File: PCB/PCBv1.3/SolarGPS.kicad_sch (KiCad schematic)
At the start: 65 parts, among them J1 Conn_01x24_Female, J2 GND, J3 GND, J4 Conn_02x03_Odd_Even, J5 Solar2+, J6 Solar1+, J7 Screw_Terminal_01x01, J8 Conn_01x04_Male, Q1 Q_NMOS_GSD, U1 STM32L011G4Ux, U2 MAX-M10Q, U3 BQ25570, U6 LIS3DH, Y1 32.768

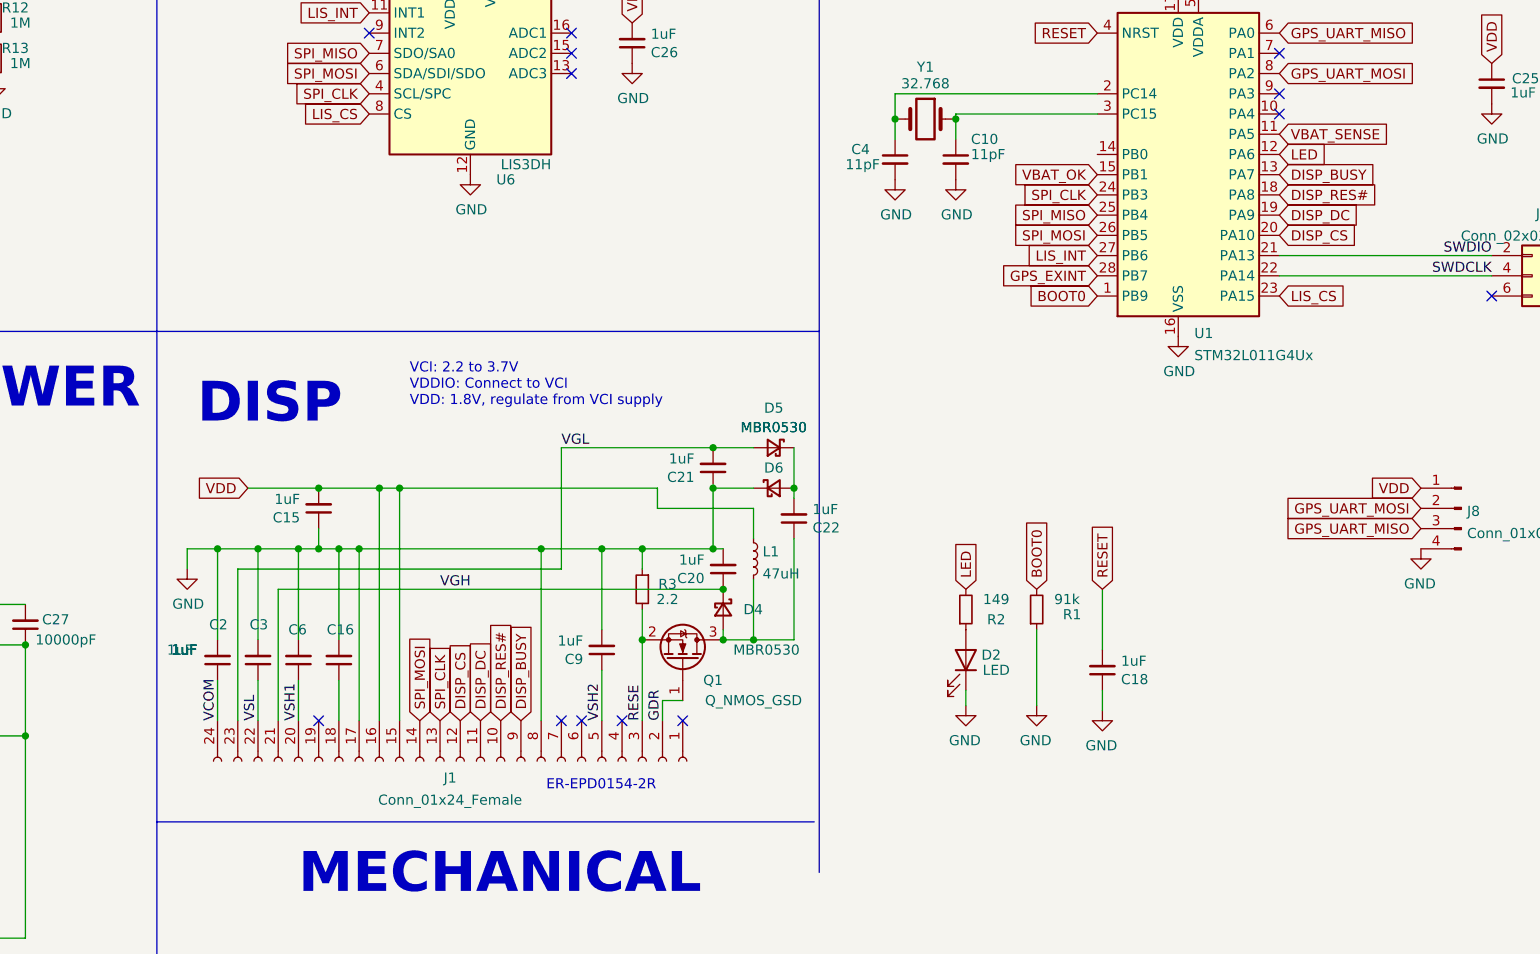
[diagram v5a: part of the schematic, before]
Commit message: Fix Reverse Epaper Connector
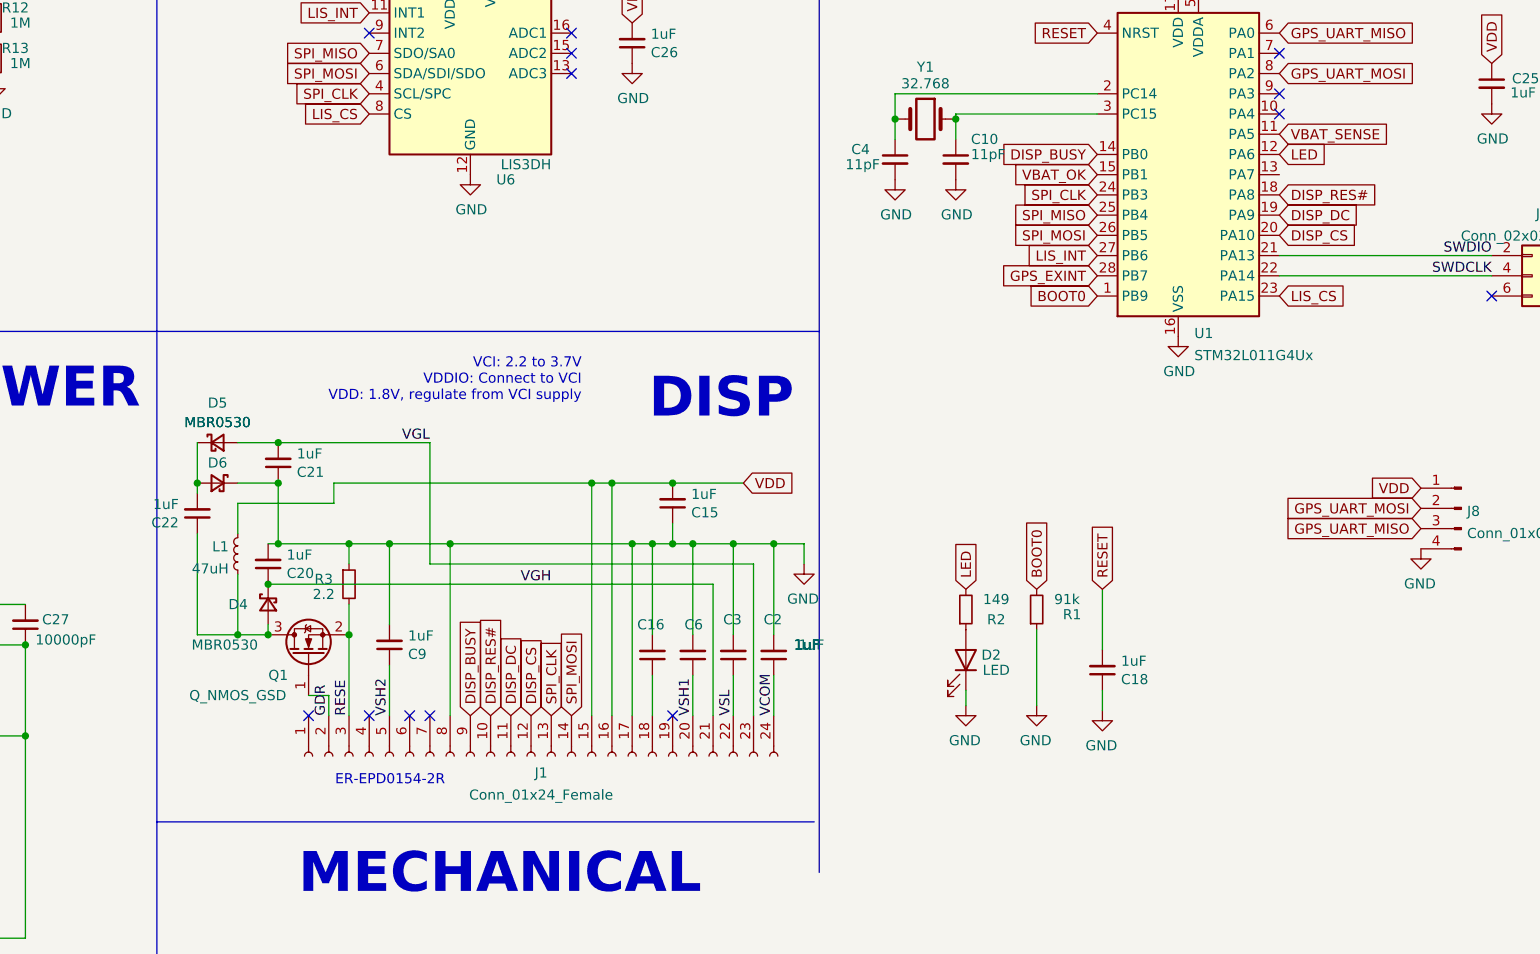
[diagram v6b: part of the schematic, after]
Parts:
- J1: footprint Connector_FFC-FPC:Hirose_FH12-24S-0.5SH_1x24-1MP_P0.50mm_Horizontal -> Heliograph:ER-CON24HT-1
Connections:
- net DISP_BUSY: now also U1.14 (PB0); no longer U1.13 (PA7)
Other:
- moved on the sheet: C15, C16, C2, C20, C21, C22, C3, C6, C9, D4, D5, D6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
